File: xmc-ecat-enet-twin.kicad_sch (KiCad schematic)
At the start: 7 parts, among them U11 UMW3157, Y2 Oscillator_25M_3225_3v3_YSO11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

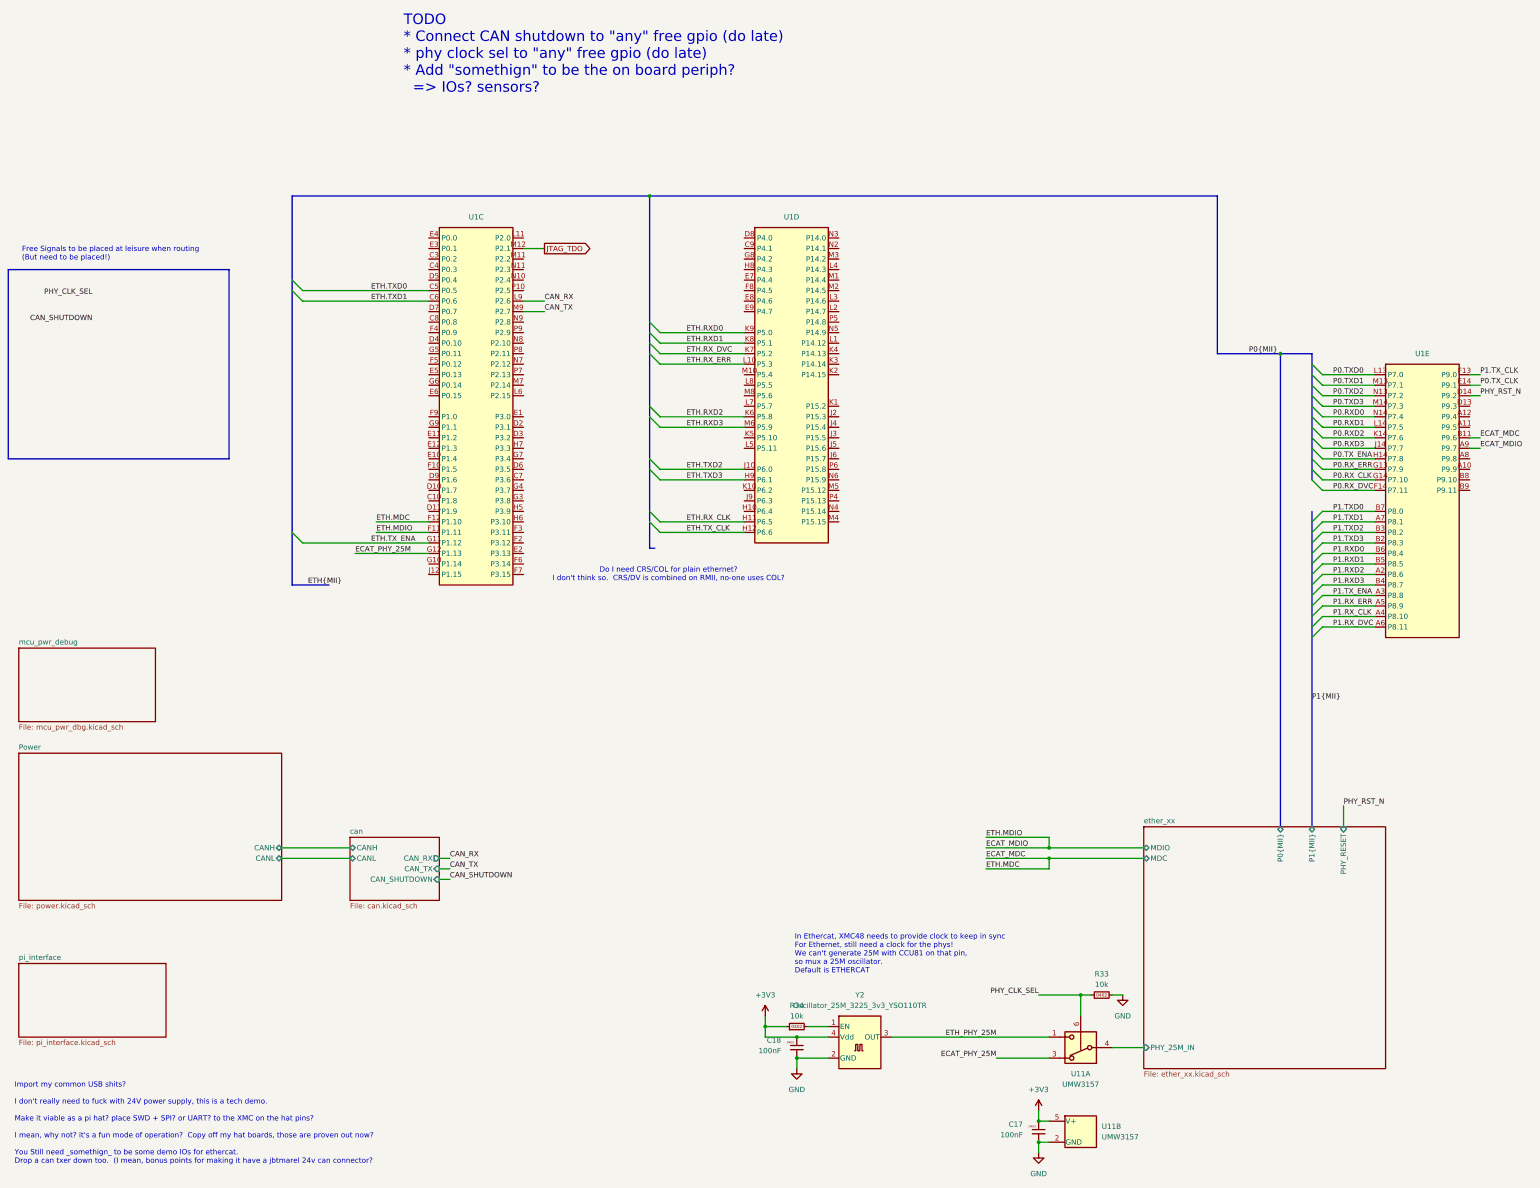
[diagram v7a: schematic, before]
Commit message: sch: clean up layout a little
just make it prettier
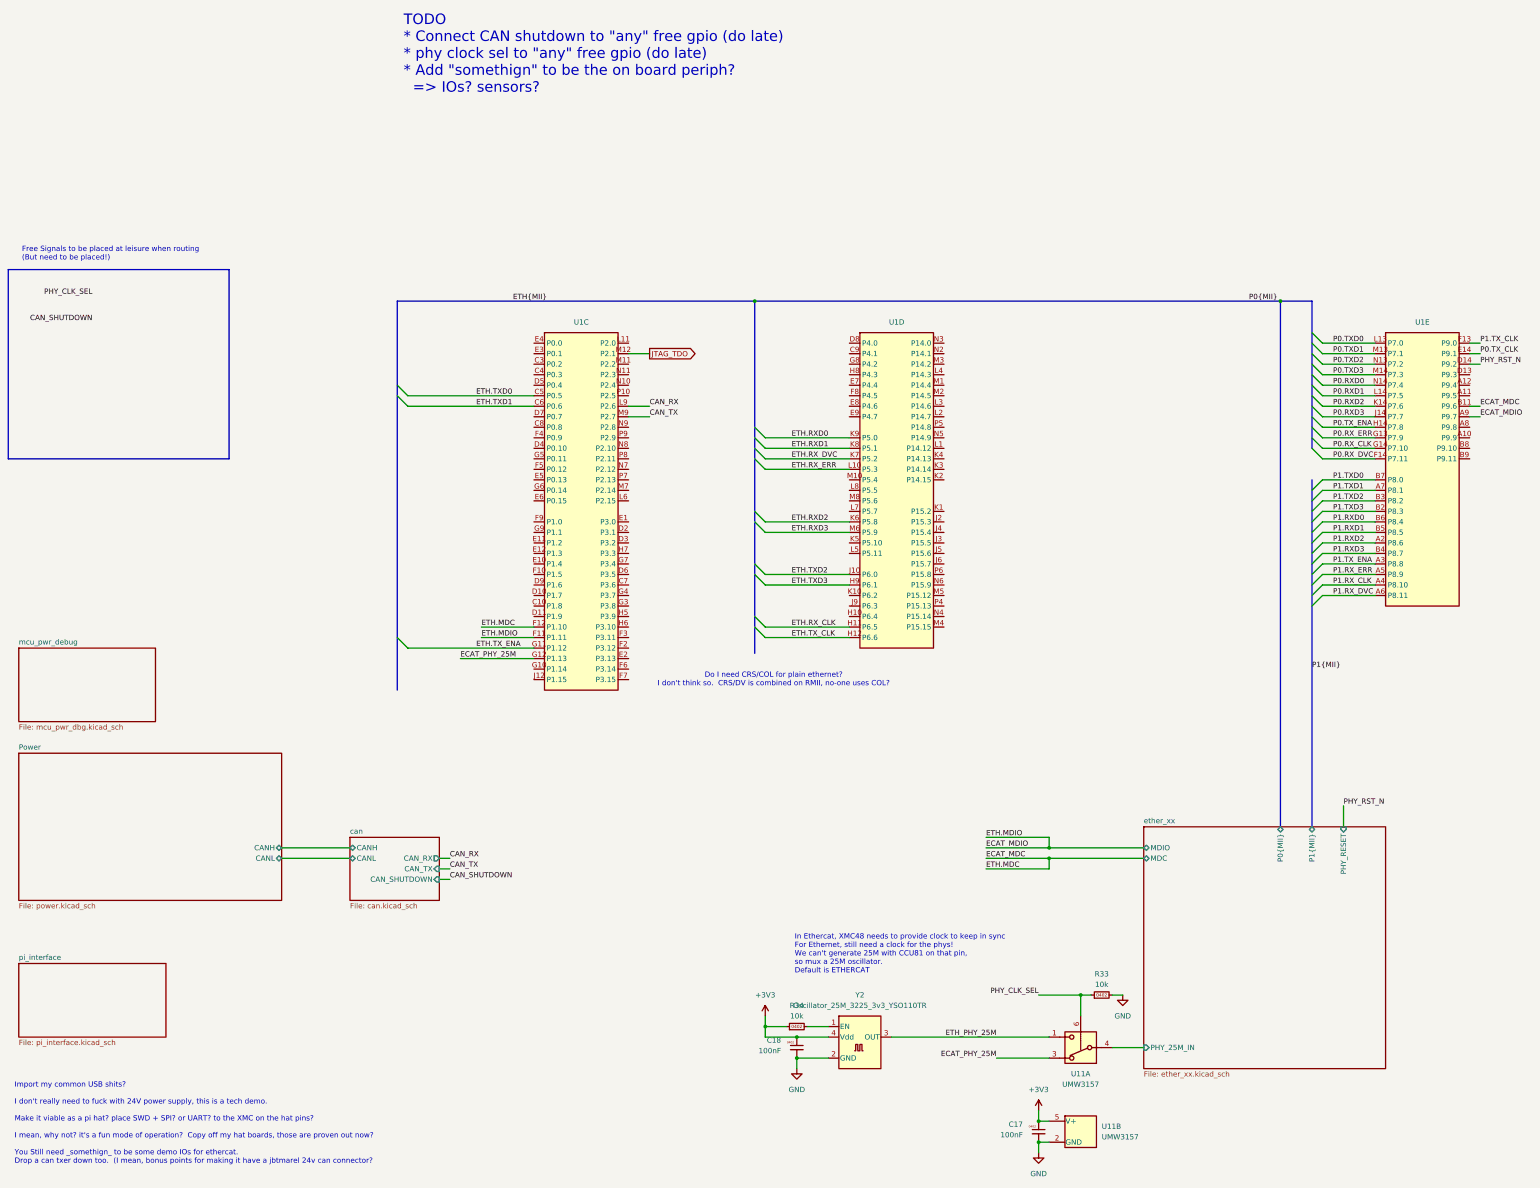
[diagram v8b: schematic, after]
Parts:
- added unit 2 of U11
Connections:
- net +3V3: now also U11.5 (V+); no longer U11.5 (V+)
- net GND: now also U11.2 (GND); no longer U11.2 (GND)
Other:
- moved on the sheet: U1C, U1D, U1E
